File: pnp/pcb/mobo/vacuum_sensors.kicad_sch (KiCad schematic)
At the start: 6 parts, among them U2 TL072, U9 MCP3426-xMS

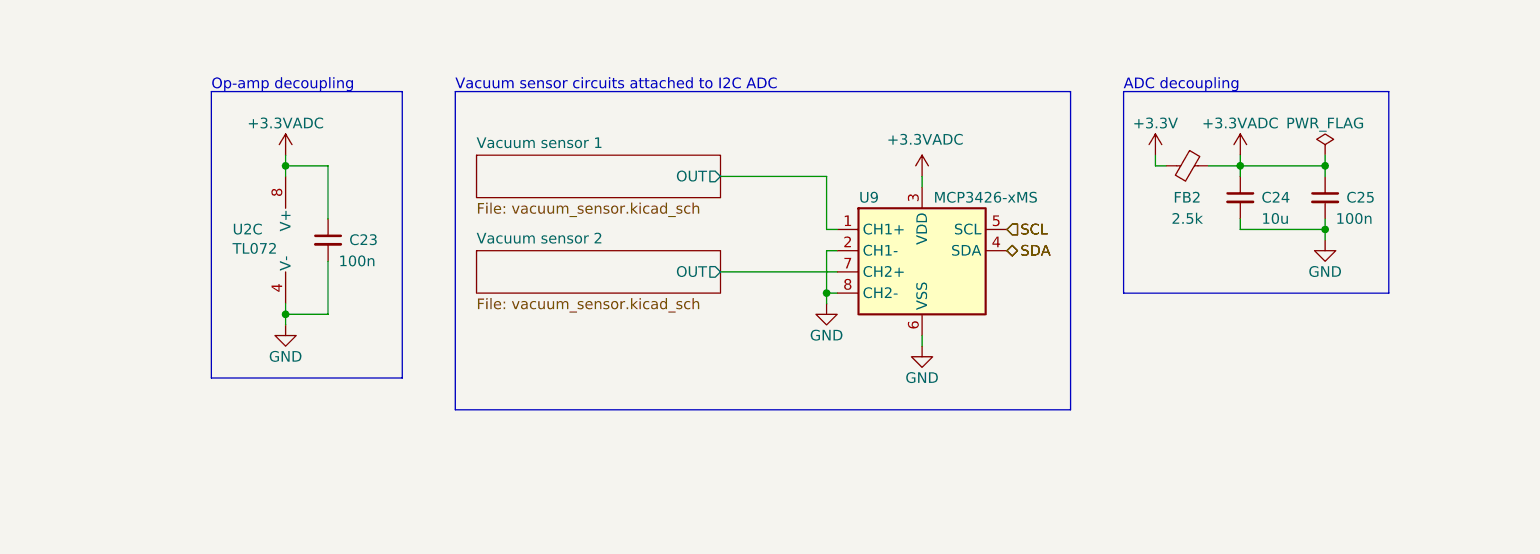
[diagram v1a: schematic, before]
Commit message: another huge chunk of work on rev04 of the mobo. breaks out diag and index pin for TMC2209 sensorless homing. reduces unique part count by consolidating resistor values where possible. replaces full ADC pipeline with monolithic I2C vacuum sensor and an I2C multiplexer due to address collision issues with two sensors. adds solder selectable jumpers for selecting whether an axis uses switch or TMC homing. redoes lots of routing of the SPI lines up to the stepper drivers.
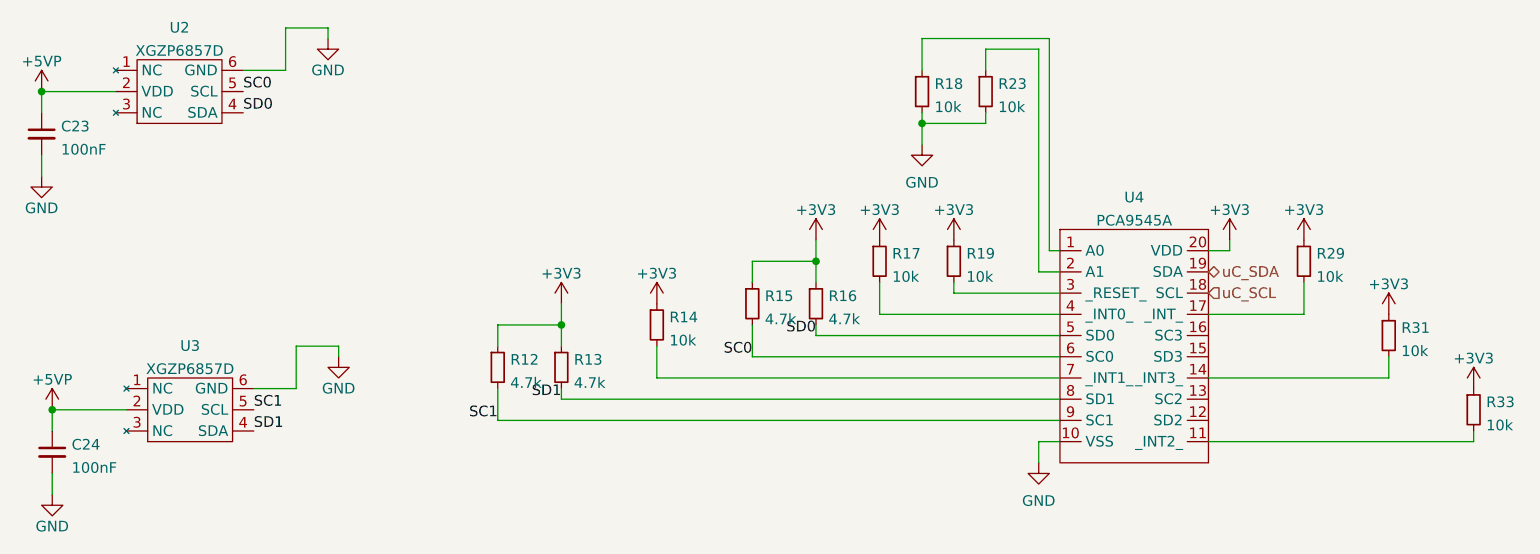
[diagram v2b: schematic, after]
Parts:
- removed C25: 100n, Capacitor_SMD:C_0805_2012Metric, symbol Device:C_Small
- removed FB2: 2.5k, Inductor_SMD:L_0805_2012Metric, symbol Device:FerriteBead_Small
- removed U2: TL072, Package_SO:SOIC-8_3.9x4.9mm_P1.27mm, symbol Amplifier_Operational:TL072
- removed U9: MCP3426-xMS, Package_SO:MSOP-8_3x3mm_P0.65mm, symbol Analog_ADC:MCP3426-xMS
- added R12, R13, R15, R16: 4.7k, Resistor_SMD:R_0805_2012Metric, symbol Device:R_Small
- added R14, R17, R18, R19, R23, R29, R31, R33: 10k, Resistor_SMD:R_0805_2012Metric, symbol Device:R_Small
- added U2, U3: XGZP6857D, index:XGZP6857D, symbol index:XGZP6857D
- added U4: PCA9545A, Package_SO:TSSOP-20_4.4x6.5mm_P0.65mm, symbol index:PCA9545A
- C23: value 100n -> 100nF; Digikey 1276-1180-1-ND -> (none); JLCPCB C49678 -> (none); LCSC C360619 -> (none); Mouser 581-08055C104K -> (none)
- C24: value 10u -> 100nF; Digikey 490-18663-1-ND -> (none); JLCPCB C15850 -> (none); LCSC C17024 -> (none); Mouser 81-GRM21BR61H106KE3L -> (none)
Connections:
- net +3V3: now also R12.1, R13.1, R14.1, R15.1, R16.1, R17.1, R19.1, R29.1, R31.1, R33.1, U4.20 (VDD)
- net GND: now also R18.2, R23.2, U2.6 (GND), U3.6 (GND), U4.10 (VSS)
- net +3.3VADC renamed +5VP
- net +5VP: now also U2.2 (VDD), U3.2 (VDD)
- new net: R31.2, U4.14 (_INT3_)
- new net: R14.2, U4.7 (_INT1_)
- new net: R23.1, U4.2 (A1)
- new net: R18.1, U4.1 (A0)
- new net: R19.2, U4.3 (_RESET_)
- new net: R33.2, U4.11 (_INT2_)
- new net: R29.2, U4.17 (_INT_)
- new net: R17.2, U4.4 (_INT0_)
- new net SC0: R15.2, U2.5 (SCL), U4.6 (SC0)
- new net SC1: R12.2, U3.5 (SCL), U4.9 (SC1)
- new net SD0: R16.2, U2.4 (SDA), U4.5 (SD0)
- new net SD1: R13.2, U3.4 (SDA), U4.8 (SD1)
- new net uC_SCL: U4.18 (SCL)
- new net uC_SDA: U4.19 (SDA)
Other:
- removed sheet Vacuum sensor 1
- removed sheet Vacuum sensor 2
- note removed: "ADC decoupling"
- note removed: "Op-amp decoupling"
- note removed: "Vacuum sensor circuits attached to I2C ADC"
- company: (none) -> Opulo
- title: Index Mobo -> LumenPnP Motherboard

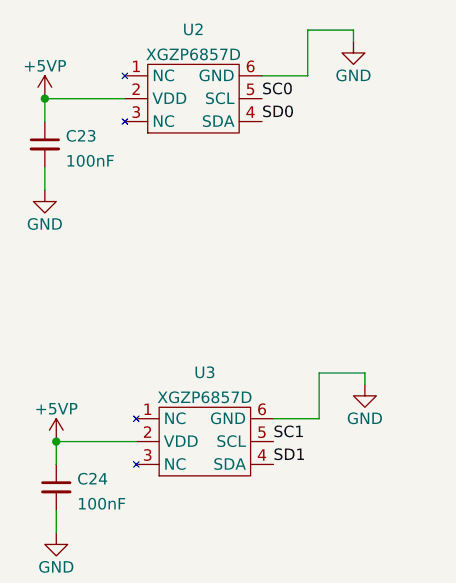
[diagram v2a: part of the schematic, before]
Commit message: adds all missing 3d models, including custom model for the vacuum sensor. corrects wrong model for the diag and index pin header for the stepper drivers. changes the vacuum sensors to 3.3v power instead of 5v. cleans up some silkscreen.
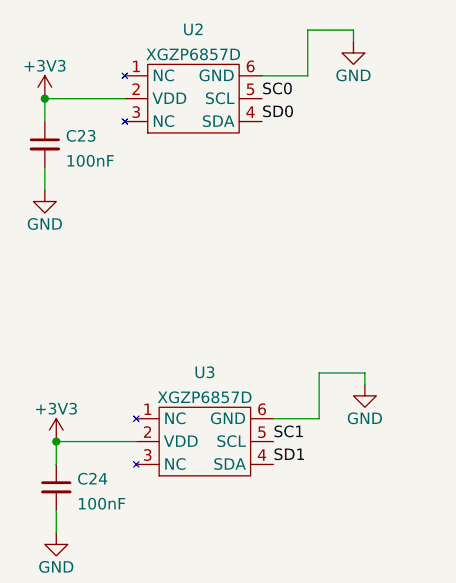
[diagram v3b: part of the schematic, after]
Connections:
- net +5VP is gone; now on net +3V3: C23.1, C24.1, U2.2 (VDD), U3.2 (VDD)
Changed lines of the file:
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@@
   (junction (at 167.64 87.63) (diameter 0) (color 0 0 0 0)
   )
+  (junction (at 124.46 111.76) (diameter 0) (color 0 0 0 0)
+  )
   (junction (at 62.23 83.82) (diameter 0) (color 0 0 0 0)
-  )
-  (junction (at 124.46 111.76) (diameter 0) (color 0 0 0 0)
   )
   (wire (pts (xy 167.64 77.47) (xy 167.64 81.28))
@@
     (pin "1")
   )
+  (symbol (lib_id "power:+3V3") (at 62.23 83.82 0) (unit 1)
+    (in_bom yes) (on_board yes) (fields_autoplaced)
+    (property "Reference" "#PWR0239" (id 0) (at 62.23 87.63 0)
+      (effects (font (size 1.27 1.27)) hide)
+    )
+    (property "Value" "+3V3" (id 1) (at 62.23 80.2155 0))
+    (property "Footprint" "" (id 2) (at 62.23 83.82 0)
+      (effects (font (size 1.27 1.27)) hide)
+    )
+    (property "Datasheet" "" (id 3) (at 62.23 83.82 0)
+      (effects (font (size 1.27 1.27)) hide)
+    )
+    (pin "1")
+  )
   (symbol (lib_id "index:XGZP6857D") (at 80.01 121.92 0) (unit 1)
     (in_bom yes) (on_board yes) (fields_autoplaced)
@@
     (pin "1")
   )
+  (symbol (lib_id "power:+3V3") (at 63.5 121.92 0) (unit 1)
+    (in_bom yes) (on_board yes) (fields_autoplaced)
+    (property "Reference" "#PWR0105" (id 0) (at 63.5 125.73 0)
+      (effects (font (size 1.27 1.27)) hide)
+    )
+    (property "Value" "+3V3" (id 1) (at 63.5 118.3155 0))
+    (property "Footprint" "" (id 2) (at 63.5 121.92 0)
+      (effects (font (size 1.27 1.27)) hide)
+    )
+    (property "Datasheet" "" (id 3) (at 63.5 121.92 0)
+      (effects (font (size 1.27 1.27)) hide)
+    )
+    (pin "1")
+  )
   (symbol (lib_id "Device:R_Small") (at 162.56 104.14 0) (unit 1)
     (in_bom yes) (on_board yes) (fields_autoplaced)
@@
     (pin "2")
   )
-  (symbol (lib_id "power:+5VP") (at 62.23 83.82 0) (unit 1)
-    (in_bom yes) (on_board yes) (fields_autoplaced)
-    (property "Reference" "#PWR0105" (id 0) (at 62.23 87.63 0)
-      (effects (font (size 1.27 1.27)) hide)
-    )
-    (property "Value" "+5VP" (id 1) (at 62.23 80.2155 0))
-    (property "Footprint" "" (id 2) (at 62.23 83.82 0)
-      (effects (font (size 1.27 1.27)) hide)
-    )
-    (property "Datasheet" "" (id 3) (at 62.23 83.82 0)
-      (effects (font (size 1.27 1.27)) hide)
-    )
-    (pin "1")
-  )
-  (symbol (lib_id "power:+5VP") (at 63.5 121.92 0) (unit 1)
-    (in_bom yes) (on_board yes) (fields_autoplaced)
-    (property "Reference" "#PWR0239" (id 0) (at 63.5 125.73 0)
-      (effects (font (size 1.27 1.27)) hide)
-    )
-    (property "Value" "+5VP" (id 1) (at 63.5 118.3155 0))
-    (property "Footprint" "" (id 2) (at 63.5 121.92 0)
-      (effects (font (size 1.27 1.27)) hide)
-    )
-    (property "Datasheet" "" (id 3) (at 63.5 121.92 0)
-      (effects (font (size 1.27 1.27)) hide)
-    )
-    (pin "1")
-  )
 )

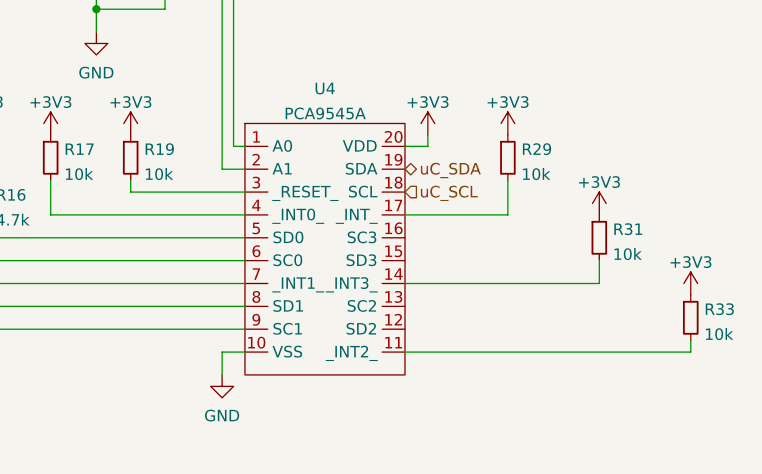
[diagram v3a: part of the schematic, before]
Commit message: fixes erc errors about pin connectivity
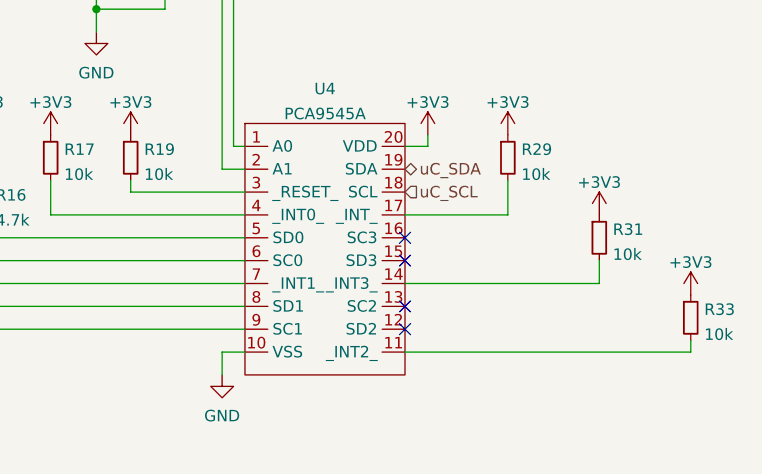
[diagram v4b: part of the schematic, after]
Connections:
- no-connect marks 0 -> 4
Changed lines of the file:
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@@
   (junction (at 62.23 83.82) (diameter 0) (color 0 0 0 0)
   )
+  (no_connect (at 201.93 113.03))
+  (no_connect (at 201.93 115.57))
+  (no_connect (at 201.93 120.65))
+  (no_connect (at 201.93 123.19))
   (wire (pts (xy 167.64 77.47) (xy 167.64 81.28))
     (stroke (width 0) (type default) (color 0 0 0 0))
